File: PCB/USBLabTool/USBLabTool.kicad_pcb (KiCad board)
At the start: 2 copper layers, 228 parts, among them J1 Conn_01x06_Pin, J10 T_pwm, J11 T_buf, J12 T_buf, J13 ADC2, J14 ADC1, J15 +3.3VA, J16 +3.3VA, J17 2x01, J19 T_N5V, J2 Conn_02x12_Odd_Even, J20 USB_C_Receptacle, J3 T_att, J4 T_att, J5 T_acdc, J6 T_acdc, J7 T_amp, J8 T_amp, J9 T_pwm, K1 G5V-2, K2 G5V-2, SW1 SW_Push, U1 AQY284SX, U10 Opamp_Quad, U11 DG403, U12 STM32H562VGTx, U13 r1283, U14 XC6206PxxxMR, U15 XC6206PxxxMR, U16 LTC1983ES6-5#TRPBF, U17 TCPP01-M12, U18 74HC245, U2 AQY284SX, U20 74HC245, U3 CD74HC4316M96, U4 LMP7718, U5 CD74HC4316M96, U6 LMP7718, U7 OPA863, U8 OPA863, U9 Opamp_Quad, Y1 32.768kHz

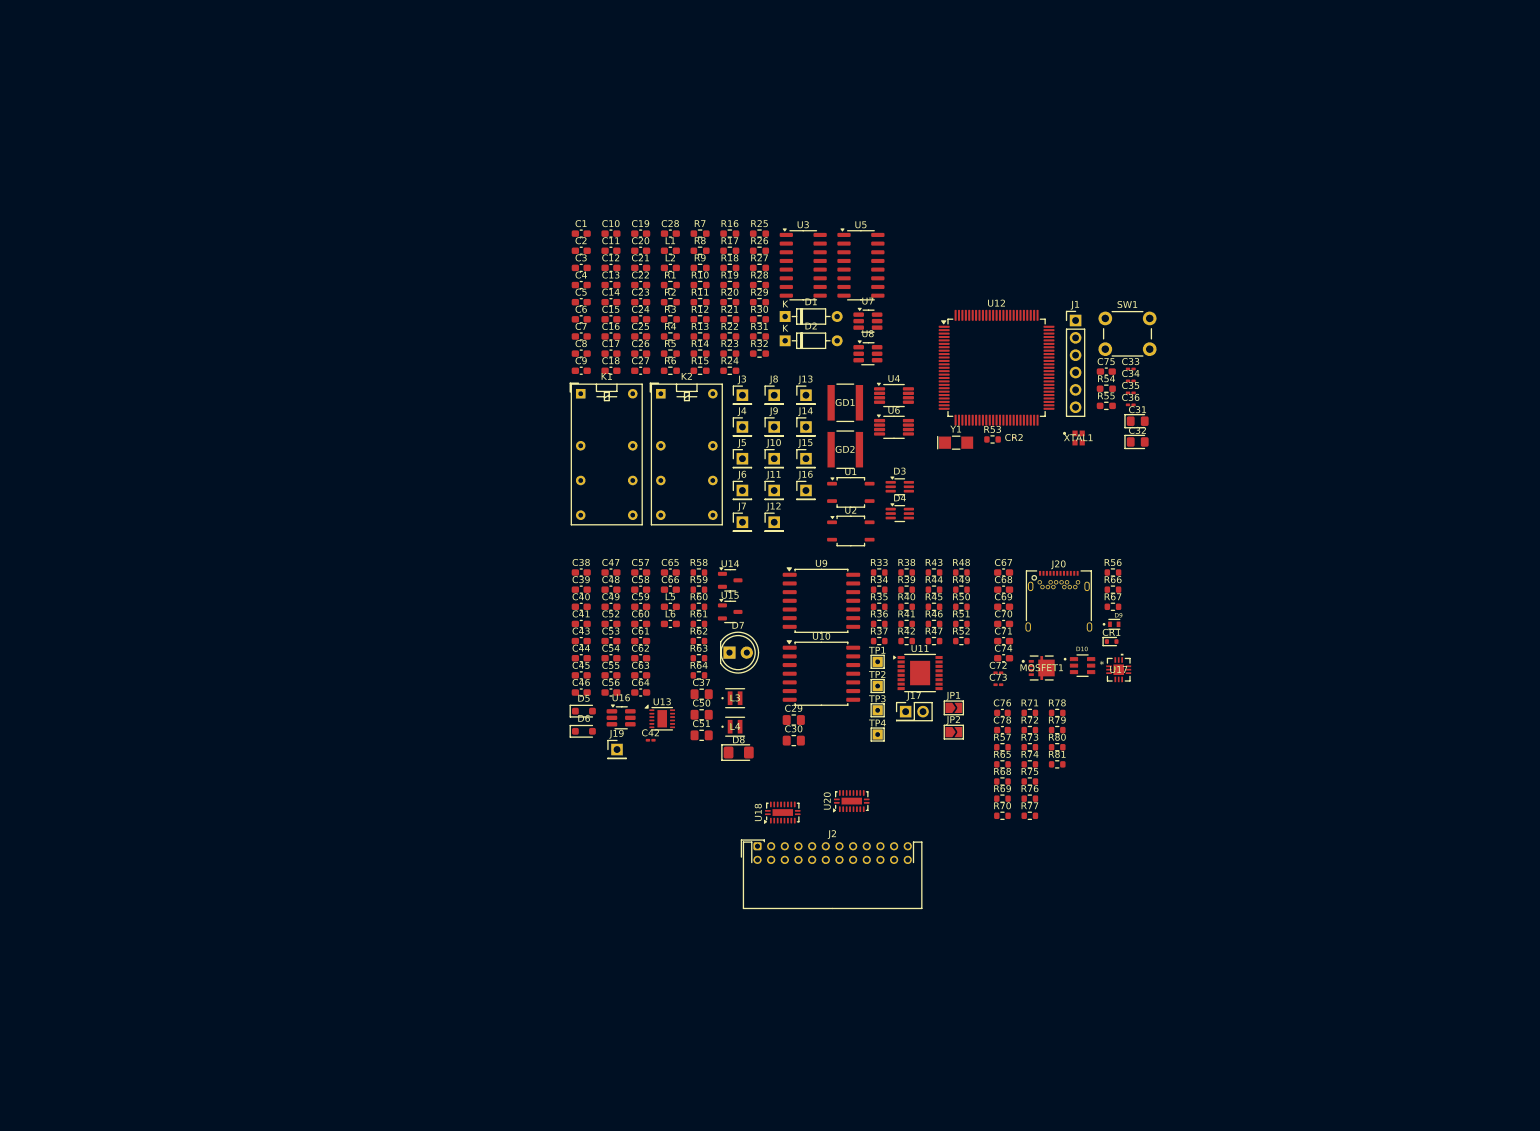
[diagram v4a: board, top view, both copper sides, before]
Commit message: Updated schematic and PCB
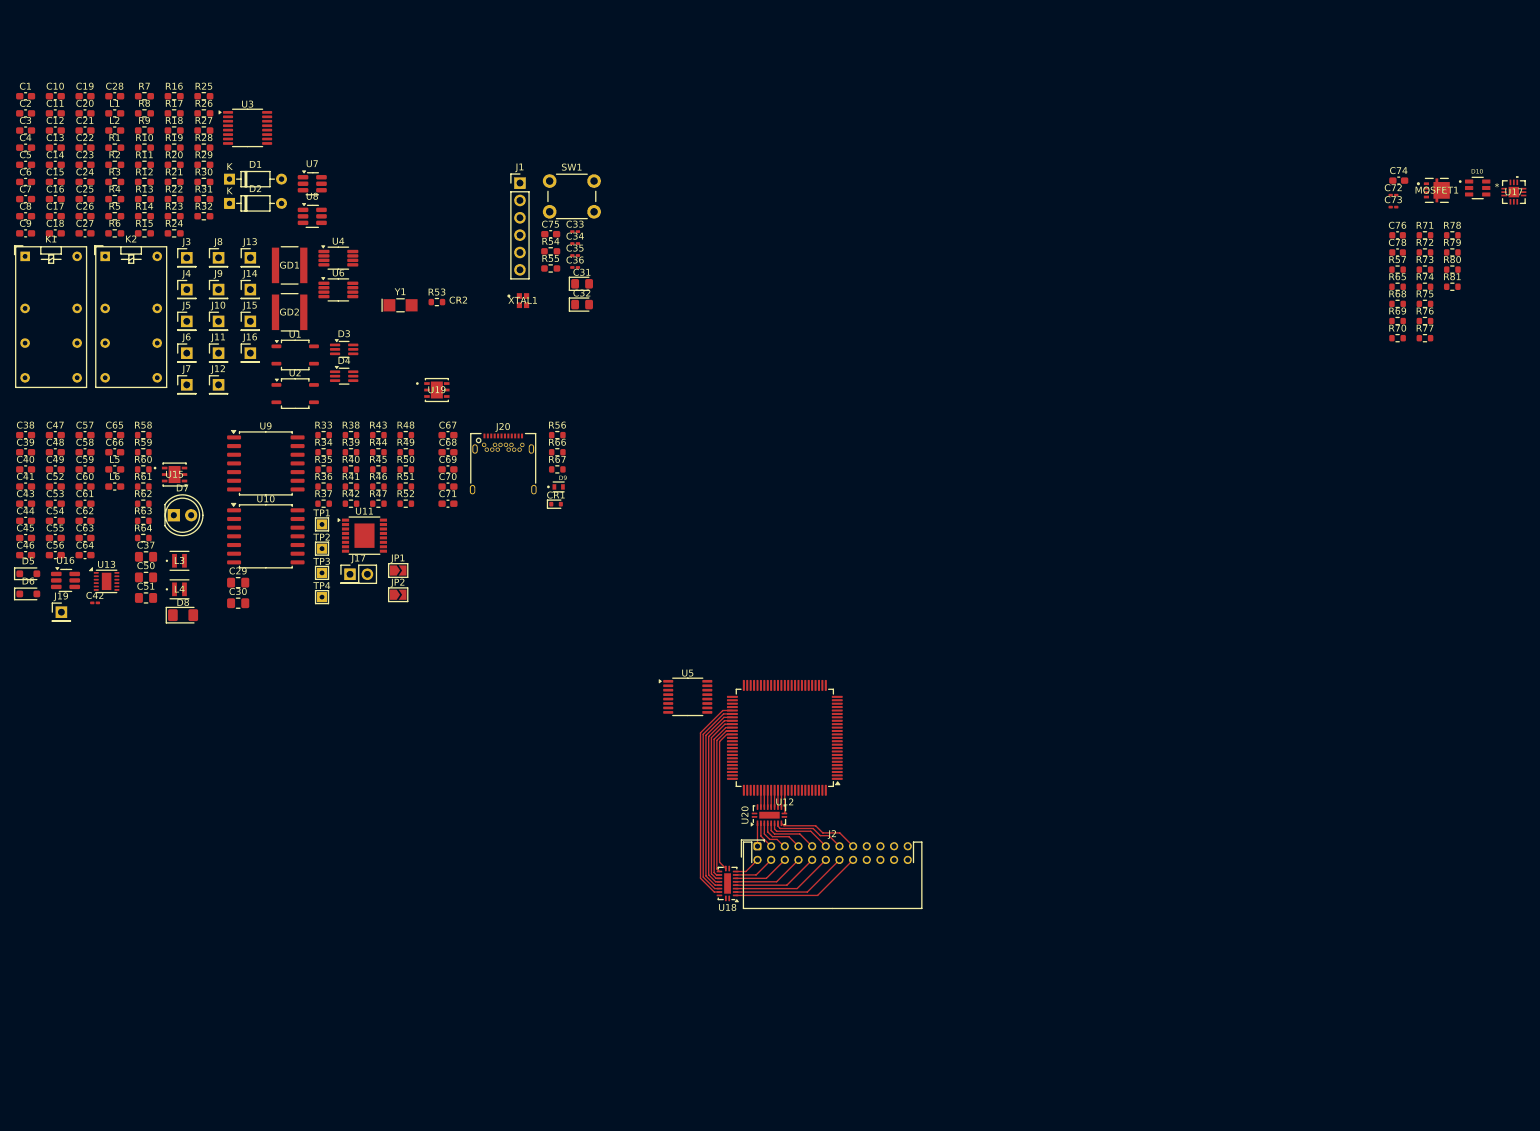
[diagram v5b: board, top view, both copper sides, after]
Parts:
- removed U14: XC6206PxxxMR, Package_TO_SOT_SMD:SOT-23-3
- added U19: ST1L05APU33R, userfp:DFN_5APU33R_STM, F.Cu at (92.2, 70.5)
- C55, C56, C58, C59, C60: value 270n -> 4.7uF
- U15: value XC6206PxxxMR -> ST1L05APU33R; footprint Package_TO_SOT_SMD:SOT-23-3 -> userfp:DFN_5APU33R_STM
- U3, U5: footprint Package_SO:SOIC-16_3.9x9.9mm_P1.27mm -> Package_SO:TSSOP-16_4.4x5mm_P0.65mm
- moved C76 90.8 mm to (232.9, 47.9)
- moved C78 90.8 mm to (232.9, 50.4)
- moved R65 90.8 mm to (232.9, 55.4)
- moved R68 90.8 mm to (232.9, 57.9)
- moved U17 90.8 mm to (249.9, 41.6)
- moved R57 90.8 mm to (232.9, 52.9)
- moved R69 90.8 mm to (232.9, 60.5)
- moved C72 90.8 mm to (232.3, 42.0)
- moved C73 90.8 mm to (232.3, 43.8)
- moved C74 90.8 mm to (233.0, 39.9)
- moved D10 90.8 mm to (244.6, 41.0)
- moved MOSFET1 90.8 mm to (238.6, 41.3)
- moved R71 90.8 mm to (236.9, 47.9)
- moved R72 90.8 mm to (236.9, 50.4)
- moved R73 90.8 mm to (236.9, 52.9)
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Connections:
- C58 pad 1: +3.3V -> GND
- C58 pad 2: GND -> +3.3V
- C59 pad 1: Net-(U15-VO) -> GNDA
- C59 pad 2: GNDA -> Net-(U15-V0)
- C60 pad 1: +3.3VA -> GNDA
- C60 pad 2: GNDA -> +3.3VA
- L5 pad 1: Net-(U15-VO) -> Net-(U15-V0)
- R57 pad 1: LOGIC_INP8 -> LOGIC_INP15
- R65 pad 2: LOGIC_INP12 -> LOGIC_INP11
- R68 pad 1: LOGIC_INP9 -> LOGIC_INP14
- R69 pad 2: LOGIC_INP13 -> LOGIC_INP10
- R70 pad 1: LOGIC_INP10 -> LOGIC_INP13
- R71 pad 2: LOGIC_INP14 -> LOGIC_INP9
- R72 pad 1: LOGIC_INP11 -> LOGIC_INP12
- R73 pad 2: LOGIC_INP15 -> LOGIC_INP8
- U12 pad 55: LOGIC_IN8 -> LOGIC_IN15
- U12 pad 56: LOGIC_IN9 -> LOGIC_IN14
- U12 pad 57: LOGIC_IN10 -> LOGIC_IN13
- U12 pad 58: LOGIC_IN11 -> LOGIC_IN12
- U12 pad 59: LOGIC_IN12 -> LOGIC_IN11
- U12 pad 60: LOGIC_IN13 -> LOGIC_IN10
- U12 pad 61: LOGIC_IN14 -> LOGIC_IN9
- U12 pad 62: LOGIC_IN15 -> LOGIC_IN8
- U15 pad 1: GNDA -> unconnected-(U15-NC-Pad1)
- U15 pad 2: Net-(U15-VO) -> Net-(U15-V0)
- U18 pad 11: LOGIC_IN15 -> LOGIC_IN8
- U18 pad 12: LOGIC_IN14 -> LOGIC_IN9
- U18 pad 13: LOGIC_IN13 -> LOGIC_IN10
- U18 pad 14: LOGIC_IN12 -> LOGIC_IN11
- U18 pad 15: LOGIC_IN11 -> LOGIC_IN12
- U18 pad 16: LOGIC_IN10 -> LOGIC_IN13
- U18 pad 17: LOGIC_IN9 -> LOGIC_IN14
- U18 pad 18: LOGIC_IN8 -> LOGIC_IN15
- U18 pad 2: LOGIC_INP8 -> LOGIC_INP15
- U18 pad 3: LOGIC_INP9 -> LOGIC_INP14
- U18 pad 4: LOGIC_INP10 -> LOGIC_INP13
- U18 pad 5: LOGIC_INP11 -> LOGIC_INP12
- U18 pad 6: LOGIC_INP12 -> LOGIC_INP11
- U18 pad 7: LOGIC_INP13 -> LOGIC_INP10
- U18 pad 8: LOGIC_INP14 -> LOGIC_INP9
- U18 pad 9: LOGIC_INP15 -> LOGIC_INP8
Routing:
- net LOGIC_IN15: track 0.00 -> 30.9 mm
- net LOGIC_IN14: track 0.00 -> 29.5 mm
- net LOGIC_IN13: track 0.00 -> 28.1 mm
- net LOGIC_IN12: track 0.00 -> 26.7 mm
- net LOGIC_IN11: track 0.00 -> 25.3 mm
- net LOGIC_IN10: track 0.00 -> 23.8 mm
- net LOGIC_IN9: track 0.00 -> 22.2 mm
- net LOGIC_IN8: track 0.00 -> 21.3 mm
- net LOGIC_INP15: track 0.00 -> 19.4 mm
- net LOGIC_INP14: track 0.00 -> 17.1 mm
- net LOGIC_INP13: track 0.00 -> 14.9 mm
- net LOGIC_INP12: track 0.00 -> 12.7 mm
- net LOGIC_INP7: track 0.00 -> 11.9 mm
- net LOGIC_INP6: track 0.00 -> 10.6 mm
- net LOGIC_INP11: track 0.00 -> 10.5 mm
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
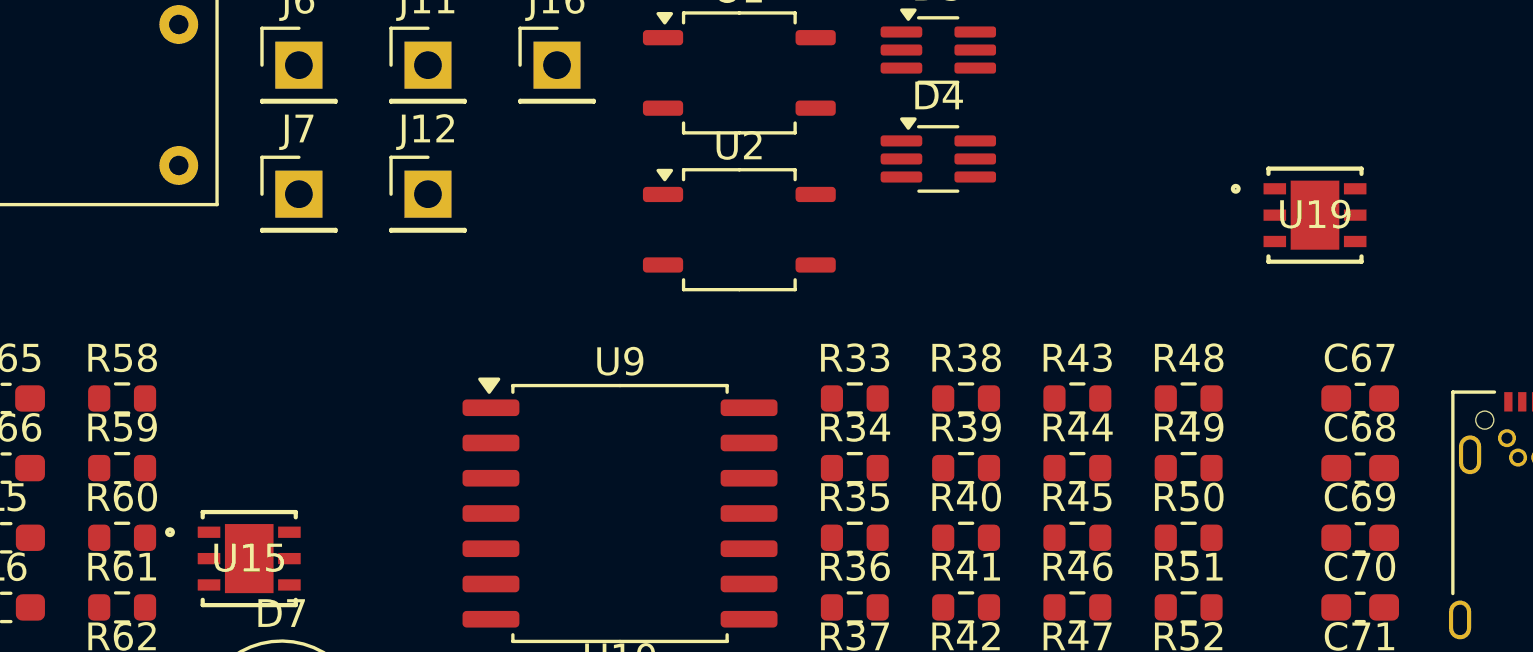
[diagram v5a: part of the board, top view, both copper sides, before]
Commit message: update ST1L05APU33R schematic
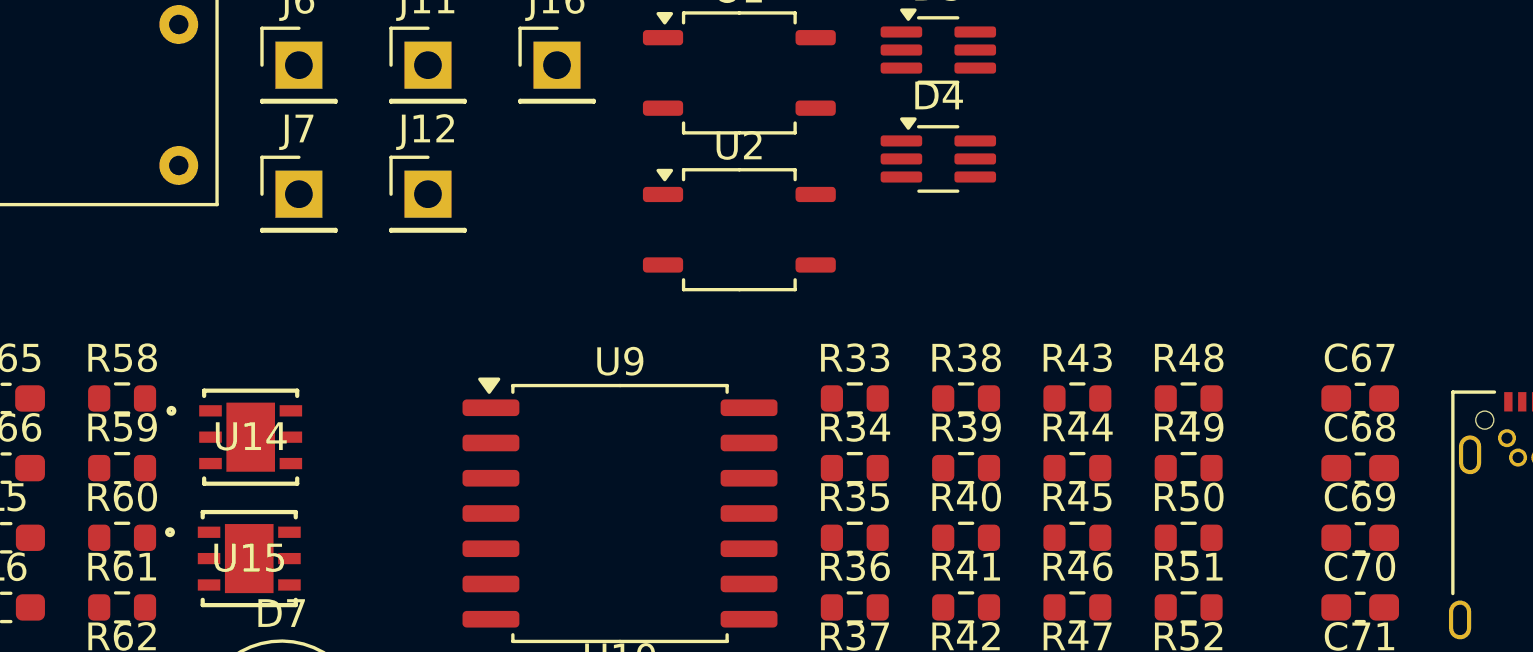
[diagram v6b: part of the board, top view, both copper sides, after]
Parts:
- removed U19: ST1L05APU33R, userfp:DFN_5APU33R_STM
- added U14: ST1L05APU33R, userfp:DFN_5APU33R_STM, F.Cu at (53.9, 78.5)
